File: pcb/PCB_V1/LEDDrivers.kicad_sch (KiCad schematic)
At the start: 57 parts, among them J711 LED1 / large 16S18P panel, J721 LED2 / strip 1, J731 LED3 / strip 2, Q711 100 V N-MOSFET / MPN pending, Q721 100 V N-MOSFET / MPN pending, Q731 100 V N-MOSFET / MPN pending, U710 LT3756, U720 LT3756, U730 LT3756

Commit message: pcb: repair LED current path and add boost energy storage
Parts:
- added C715, C725, C735: 22u / 25 V X7R / effective >=10u, Capacitor_SMD:C_1210_3225Metric, symbol Device:C
- added C716, C717, C726, C727, C736, C737: 10u / 100 V X7R / effective >=4.7u, Capacitor_SMD:C_1210_3225Metric, symbol Device:C
- C712, C722, C732: value 2.2u / 16 V -> 4.7u / 16 V X7R; footprint Capacitor_SMD:C_0603_1608Metric -> Capacitor_SMD:C_0805_2012Metric
- R711, R721, R731: value 20k / ~500 kHz preliminary -> 21k / 500 kHz nominal
- R712, R722, R732: value 10k -> 33k / CTRL upper
- R713, R723, R733: value 10k -> 100k / CTRL lower
- R715: value 0.1 / current limit sense -> 0.012 / 1% / >=2W
- R725, R735: value 0.1 / current limit sense -> 0.047 / 1% / >=1W; footprint Resistor_SMD:R_0603_1608Metric -> Resistor_SMD:R_2512_6332Metric
- U710, U720, U730: value LT3756 -> LT3756EMSE-2#PBF
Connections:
- net LED1_SENSE_P is gone; now on net LED1_OUT: R716.1, U710.4 (ISP)
- net LED2_SENSE_P is gone; now on net LED2_OUT: R726.1, U720.4 (ISP)
- net LED3_SENSE_P is gone; now on net LED3_OUT: R736.1, U730.4 (ISP)
- net +12V_LED: now also C715.1, C725.1, C735.1
- net GND: now also C715.2, C716.2, C717.2, C725.2, C726.2, C727.2, C735.2, C736.2, C737.2
- net LED1_OUT: now also C716.1, C717.1
- net LED2_OUT: now also C726.1, C727.1
- net LED3_OUT: now also C736.1, C737.1

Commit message: pcb: correct power MOSFET pin mapping and reverse input protection
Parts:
- Q711, Q721, Q731: symbol Transistor_FET:Q_NMOS_GDS -> GrowBox:NMOS_PowerPAK_Candidate
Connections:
- net LED1_GATE: now also Q711.4 (G); no longer Q711.1 (G)
- net LED1_IS: now also Q711.1 (S), Q711.2 (S)
- net LED1_SW: now also Q711.5 (D); no longer Q711.2 (D)
- net LED2_GATE: now also Q721.4 (G); no longer Q721.1 (G)
- net LED2_IS: now also Q721.1 (S), Q721.2 (S)
- net LED2_SW: now also Q721.5 (D); no longer Q721.2 (D)
- net LED3_GATE: now also Q731.4 (G); no longer Q731.1 (G)
- net LED3_IS: now also Q731.1 (S), Q731.2 (S)
- net LED3_SW: now also Q731.5 (D); no longer Q731.2 (D)
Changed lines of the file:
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@@
 		(title "07 - Three independent LED constant-current boost channels")
 		(date "2026-09-26")
-		(rev "0.6-DRAFT")
+		(rev "0.7-DRAFT")
 		(company "GrowBox controller")
 		(comment 1 "Logic first; power loads not yet implemented")
@@
 	)
 	(symbol
-		(lib_id "Transistor_FET:Q_NMOS_GDS")
+		(lib_id "GrowBox:NMOS_PowerPAK_Candidate")
 		(at 121.92 114.3 0)
 		(unit 1)
@@
 			)
 		)
+		(pin "4"
+		)
+		(pin "5"
+		)
 		(pin "1"
 		)
@@
 	)
 	(symbol
-		(lib_id "Transistor_FET:Q_NMOS_GDS")
+		(lib_id "GrowBox:NMOS_PowerPAK_Candidate")
 		(at 121.92 289.56 0)
 		(unit 1)
@@
 			)
 		)
+		(pin "4"
+		)
+		(pin "5"
+		)
 		(pin "1"
 		)
@@
 	)
 	(symbol
-		(lib_id "Transistor_FET:Q_NMOS_GDS")
+		(lib_id "GrowBox:NMOS_PowerPAK_Candidate")
 		(at 121.92 464.82 0)
 		(unit 1)
@@
 			)
 		)
+		(pin "4"
+		)
+		(pin "5"
+		)
 		(pin "1"

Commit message: pcb: match LED MOSFET packages and export complete schematic BOM
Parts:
- Q711, Q721, Q731: value 100 V N-MOSFET / MPN pending -> Si7454DDP-T1-GE3; footprint Package_SO:PowerPAK_SO-8L_Single -> Package_SO:PowerPAK_SO-8_Single
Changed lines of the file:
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@@
 			)
 		)
-		(property "Value" "100 V N-MOSFET / MPN pending"
+		(property "Value" "Si7454DDP-T1-GE3"
 			(at 121.92 104.14 0)
 			(show_name no)
@@
 			)
 		)
-		(property "Footprint" "Package_SO:PowerPAK_SO-8L_Single"
+		(property "Footprint" "Package_SO:PowerPAK_SO-8_Single"
 			(at 121.92 114.3 0)
 			(hide yes)
@@
 			)
 		)
-		(property "Datasheet" ""
+		(property "Datasheet" "https://www.vishay.com/docs/67883/si7454ddp.pdf"
 			(at 121.92 114.3 0)
 			(hide yes)
@@
 			)
 		)
-		(property "Value" "100 V N-MOSFET / MPN pending"
+		(property "Value" "Si7454DDP-T1-GE3"
 			(at 121.92 279.4 0)
 			(show_name no)
@@
 			)
 		)
-		(property "Footprint" "Package_SO:PowerPAK_SO-8L_Single"
+		(property "Footprint" "Package_SO:PowerPAK_SO-8_Single"
 			(at 121.92 289.56 0)
 			(hide yes)
@@
 			)
 		)
-		(property "Datasheet" ""
+		(property "Datasheet" "https://www.vishay.com/docs/67883/si7454ddp.pdf"
 			(at 121.92 289.56 0)
 			(hide yes)
@@
 			)
 		)
-		(property "Value" "100 V N-MOSFET / MPN pending"
+		(property "Value" "Si7454DDP-T1-GE3"
 			(at 121.92 454.66 0)
 			(show_name no)
@@
 			)
 		)
-		(property "Footprint" "Package_SO:PowerPAK_SO-8L_Single"
+		(property "Footprint" "Package_SO:PowerPAK_SO-8_Single"
 			(at 121.92 464.82 0)
 			(hide yes)
@@
 			)
 		)
-		(property "Datasheet" ""
+		(property "Datasheet" "https://www.vishay.com/docs/67883/si7454ddp.pdf"
 			(at 121.92 464.82 0)
 			(hide yes)

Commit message: pcb: replace LT3756 with lower-cost AL8853 LED channels
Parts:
- removed R710, R720, R730: 6.34k / FB divider, Resistor_SMD:R_0603_1608Metric, symbol Device:R
- removed R719, R729, R739: 249k / FB divider, Resistor_SMD:R_0603_1608Metric, symbol Device:R
- added C700: 100n 16V, Capacitor_SMD:C_0603_1608Metric, symbol Device:C
- added R701, R702, R703: 47k, Resistor_SMD:R_0603_1608Metric, symbol Device:R
- added U700: SN74LVC1G08DBVR, Package_TO_SOT_SMD:SOT-23-5, symbol 74xGxx:74LVC1G08
- C711, C721, C731: value 100n / 25 V -> 1u 25V X7R; footprint Capacitor_SMD:C_0603_1608Metric -> Capacitor_SMD:C_0805_2012Metric
- C712, C722, C732: value 4.7u / 16 V X7R -> 100p / comp tune; footprint Capacitor_SMD:C_0805_2012Metric -> Capacitor_SMD:C_0603_1608Metric
- C713, C723, C733: value 100n soft-start -> 100p / CS tune
- C714, C724, C734: value 2.2n compensation -> 220n / comp tune
- C715, C725, C735: value 22u / 25 V X7R / effective >=10u -> 22u 25V X7R
- C716, C717, C726, C727, C736, C737: value 10u / 100 V X7R / effective >=4.7u -> 10u 100V X7R
- D711, D721, D731: value 100 V Schottky / MPN pending -> 100V 5A / MPN TBD
- J711: value LED1 / large 16S18P panel -> LED +/- (return isolated); footprint TerminalBlock_WAGO:TerminalBlock_WAGO_2601-1102_1x02_P3.50mm_Horizontal -> TerminalBlock_Phoenix:TerminalBlock_Phoenix_MKDS-1,5-2-5.08_1x02_P5.08mm_Horizontal
- J721: value LED2 / strip 1 -> LED +/- (return isolated); footprint TerminalBlock_WAGO:TerminalBlock_WAGO_2601-1102_1x02_P3.50mm_Horizontal -> TerminalBlock_Phoenix:TerminalBlock_Phoenix_MKDS-1,5-2-5.08_1x02_P5.08mm_Horizontal
- J731: value LED3 / strip 2 -> LED +/- (return isolated); footprint TerminalBlock_WAGO:TerminalBlock_WAGO_2601-1102_1x02_P3.50mm_Horizontal -> TerminalBlock_Phoenix:TerminalBlock_Phoenix_MKDS-1,5-2-5.08_1x02_P5.08mm_Horizontal
- L711: value 22uH / Isat >= 10 A -> 47u / Isat>=14A / TBD; footprint Inductor_SMD:L_10.4x10.4_H4.8 -> Inductor_SMD:L_Bourns_SRP1245A
- L721, L731: value 47uH / Isat >= 3 A -> 100u / Isat>=5A / TBD; footprint Inductor_SMD:L_10.4x10.4_H4.8 -> Inductor_SMD:L_Bourns_SRP1245A
- Q711: value Si7454DDP-T1-GE3 -> SiR106ADP-T1-RE3
- R711, R721, R731: value 21k / 500 kHz nominal -> 10R
- R712, R722, R732: value 33k / CTRL upper -> 1k / slope tune
- R713, R723, R733: value 100k / CTRL lower -> 100k
- R714, R724, R734: value 10k -> 10k / comp tune
- R715: value 0.012 / 1% / >=2W -> 0.027 1% >=2W
- R716: value 0.091 / 1% -> 0.182 1% >=1W
- R717, R727, R737: value 249k / OVP divider -> 316k 1%
- R718, R728, R738: value 6.34k / OVP divider -> 10k 1%
- R725, R735: value 0.047 / 1% / >=1W -> 0.10 1% >=1W
- R726, R736: value 0.40 / 1% -> 0.80 1% >=0.25W; footprint Resistor_SMD:R_0603_1608Metric -> Resistor_SMD:R_1206_3216Metric
- U710, U720, U730: value LT3756EMSE-2#PBF -> AL8853S-13; footprint Package_SO:MSOP-16-1EP_3x4.039mm_P0.5mm_EP1.651x2.845mm_ThermalVias -> Package_SO:SOIC-8_3.9x4.9mm_P1.27mm; symbol Driver_LED:LT3756xMSE -> GrowBox:AL8853
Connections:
- net +12V_LED: now also U710.1 (VIN), U720.1 (VIN), U730.1 (VIN); no longer U710.14 (VIN), U720.14 (VIN), U730.14 (VIN)
- net GND: now also R716.2, R726.2, R736.2, U710.3 (GND), U720.3 (GND), U730.3 (GND), C700.2, R701.2, R702.2, R703.2, U700.3 (GND); no longer J711.2 (Pin_2), J721.2 (Pin_2), J731.2 (Pin_2), R711.2, R713.2, R721.2, R723.2, R731.2, R733.2, U710.17 (GND), U720.17 (GND), U730.17 (GND)
- net LED1_COMP: now also C712.1, U710.6 (COMP); no longer U710.5 (VC)
- net LED1_GATE: now also R711.2, R713.1; no longer U710.16 (GATE)
- net LED1_OUT: now also J711.1 (Pin_1); no longer R716.1, U710.4 (ISP)
- net LED1_OVP: now also U710.7 (OVP)
- net LED2_COMP: now also C722.1, U720.6 (COMP); no longer U720.5 (VC)
- net LED2_GATE: now also R721.2, R723.1; no longer U720.16 (GATE)
- net LED2_OUT: now also J721.1 (Pin_1); no longer R726.1, U720.4 (ISP)
- net LED2_OVP: now also U720.7 (OVP)
- net LED3_COMP: now also C732.1, U730.6 (COMP); no longer U730.5 (VC)
- net LED3_GATE: now also R731.2, R733.1; no longer U730.16 (GATE)
- net LED3_OUT: now also J731.1 (Pin_1); no longer R736.1, U730.4 (ISP)
- net LED3_OVP: now also U730.7 (OVP)
- net LIGHT_ENABLE: now also R702.1, U700.2; no longer U710.12 (~{SHDN}/UVLO), U720.12 (~{SHDN}/UVLO), U730.12 (~{SHDN}/UVLO)
- net LIGHT_PWM: now also R701.1, U700.1; no longer U710.8 (PWM), U720.8 (PWM), U730.8 (PWM)
- removed net LED1_CTRL: R712.2, R713.1, U710.6 (CTRL)
- net LED1_FB renamed LED1_DRV
- net LED1_DRV: now also R711.1
- removed net LED1_INTVCC: C712.1, U710.13 (INTVCC)
- net LED1_IS renamed LED1_SOURCE
- net LED1_SOURCE: now also R712.1, R713.2; no longer U710.15 (SENSE)
- removed net LED1_LEDPLUS: J711.1 (Pin_1), R716.2, U710.3 (ISN)
- removed net LED1_RT: R711.1, U710.11 (RT)
- net LED1_SS renamed LED1_CS
- net LED1_CS: now also R712.2, U710.4 (CS); no longer U710.10 (SS)
- removed net LED1_VREF: R712.1, U710.7 (VREF)
- removed net LED2_CTRL: R722.2, R723.1, U720.6 (CTRL)
- net LED2_FB renamed LED2_DRV
- net LED2_DRV: now also R721.1
- removed net LED2_INTVCC: C722.1, U720.13 (INTVCC)
- net LED2_IS renamed LED2_SOURCE
- net LED2_SOURCE: now also R722.1, R723.2; no longer U720.15 (SENSE)
- removed net LED2_LEDPLUS: J721.1 (Pin_1), R726.2, U720.3 (ISN)
- removed net LED2_RT: R721.1, U720.11 (RT)
- net LED2_SS renamed LED2_CS
- net LED2_CS: now also R722.2, U720.4 (CS); no longer U720.10 (SS)
- removed net LED2_VREF: R722.1, U720.7 (VREF)
- removed net LED3_CTRL: R732.2, R733.1, U730.6 (CTRL)
- net LED3_FB renamed LED3_DRV
- net LED3_DRV: now also R731.1
- removed net LED3_INTVCC: C732.1, U730.13 (INTVCC)
- net LED3_IS renamed LED3_SOURCE
- net LED3_SOURCE: now also R732.1, R733.2; no longer U730.15 (SENSE)
- removed net LED3_LEDPLUS: J731.1 (Pin_1), R736.2, U730.3 (ISN)
- removed net LED3_RT: R731.1, U730.11 (RT)
- net LED3_SS renamed LED3_CS
- net LED3_CS: now also R732.2, U730.4 (CS); no longer U730.10 (SS)
- removed net LED3_VREF: R732.1, U730.7 (VREF)
- new net +3V3: C700.1, U700.5 (VCC)
- new net LED1_RETURN: J711.2 (Pin_2), R716.1, U710.5 (FB)
- new net LED2_RETURN: J721.2 (Pin_2), R726.1, U720.5 (FB)
- new net LED3_RETURN: J731.2 (Pin_2), R736.1, U730.5 (FB)
- new net LED_DIM: R703.1, U700.4, U710.8 (PWM), U720.8 (PWM), U730.8 (PWM)
- no-connect marks 6 -> 0
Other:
- note added: "0.9 COST-DOWN DRAFT: component budget <= USD 30 target, not a purchase quote. AL8853 replaces LT3756."
- note added: "CH1: 1.099 A nominal / panel"
- note added: "CH2: 0.250 A nominal / strip"
- note added: "CH3: 0.250 A nominal / strip"
- note added: "DRAFT: 120 kHz; OVP nominal 65.2 V. All output power parts >=100 V. Inductor/diode footprints are placeholders."
- note added: "Do not connect LED- to GND or join LED returns. Output short protection needs branch fuses/disconnect; boost diode conducts at shutdown."
- note added: "L saturation/current rating, slope compensation, transient response, output capacitance and thermal performance require verification."
- note added: "PWM 20 kHz initial / analog current dimming. Enable low or reset: DIM low. LED returns MUST remain separate."
- note added: "THREE INDEPENDENT CONSTANT-CURRENT BOOST CHANNELS / COMMON DIMMING"
- note removed: "0.4 DRAFT. Target currents: CH1 1.10 A, CH2 0.25 A, CH3 0.25 A; total nominal 76.8 W at 48 V."
- note removed: "All three channels share LIGHT_PWM and LIGHT_ENABLE from ESP32 but have independent inductors, MOSFETs, current-sense resistors, OVP and LED connectors. Keep switch loops compact and separate from SENSE/FB routing."
- note removed: "CHANNEL 1: large 16S18P panel / 1.10 A target / 52.8 W target"
- note removed: "CHANNEL 2: strip 1 / 0.25 A target / 12.0 W target"
- note removed: "CHANNEL 3: strip 2 / 0.25 A target / 12.0 W target"
- note removed: "LED / 12 V -> 40..48 V / THREE INDEPENDENT CONSTANT-CURRENT BOOST CHANNELS"
- note removed: "RCS 0.091 / 1%; high-side shunt before LED+. Tune after measuring actual LED Vf and current. R715 is switch-current sense, not LED current sense. OVP/FB dividers are preliminary for 48 V operation; validate open-LED overshoot and compensation with the real panel."
- note removed: "RCS 0.40 / 1%; high-side shunt before LED+. Tune after measuring actual LED Vf and current. R725 is switch-current sense, not LED current sense. OVP/FB dividers are preliminary for 48 V operation; validate open-LED overshoot and compensation with the real panel."
- note removed: "RCS 0.40 / 1%; high-side shunt before LED+. Tune after measuring actual LED Vf and current. R735 is switch-current sense, not LED current sense. OVP/FB dividers are preliminary for 48 V operation; validate open-LED overshoot and compensation with the real panel."
- title: 07 - Three independent LED constant-current boost channels -> 07 - AL8853 cost-down LED drivers
- moved on the sheet: C711, C712, C713, C714, C715, C716, C717, C721, C722, C723, C724, C725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

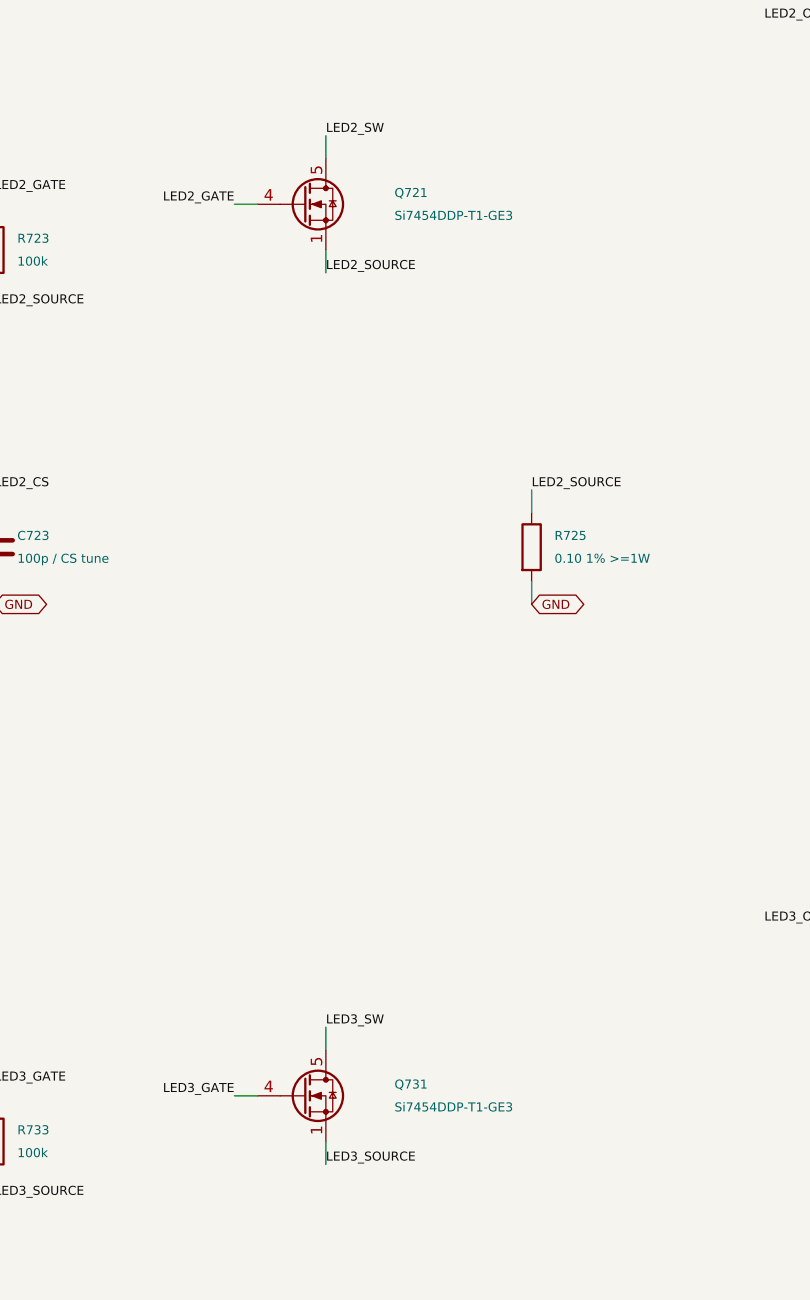
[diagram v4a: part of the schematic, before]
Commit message: pcb: replace strip LED MOSFETs with DMT10H009LK3 DPAK parts
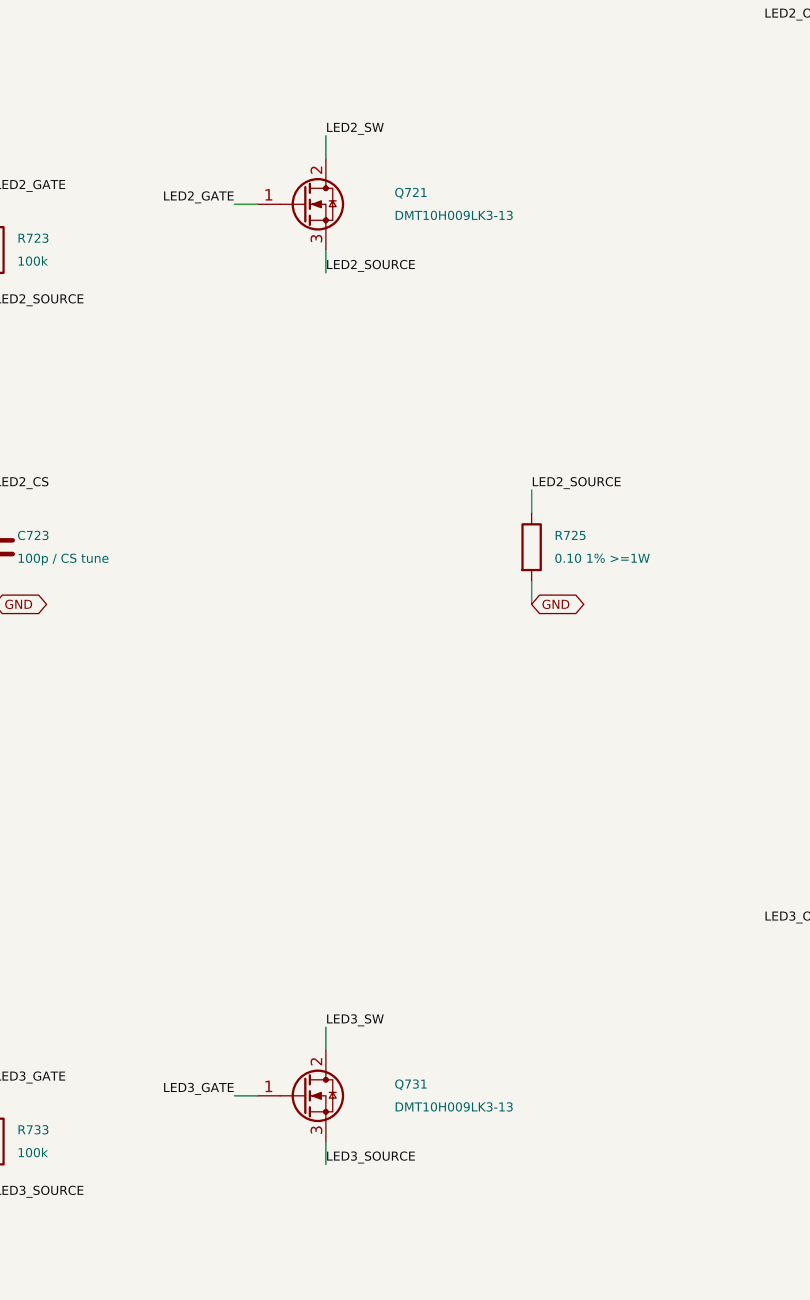
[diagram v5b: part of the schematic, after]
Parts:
- Q721, Q731: value Si7454DDP-T1-GE3 -> DMT10H009LK3-13; footprint Package_SO:PowerPAK_SO-8_Single -> GrowBox:Diodes_TO252_DMT10H009LK3; symbol GrowBox:NMOS_PowerPAK_Candidate -> GrowBox:DMT10H009LK3
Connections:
- net LED2_GATE: now also Q721.1 (G); no longer Q721.4 (G)
- net LED2_SOURCE: no longer Q721.1 (S), Q721.2 (S)
- net LED2_SW: now also Q721.2 (D); no longer Q721.5 (D)
- net LED3_GATE: now also Q731.1 (G); no longer Q731.4 (G)
- net LED3_SOURCE: no longer Q731.1 (S), Q731.2 (S)
- net LED3_SW: now also Q731.2 (D); no longer Q731.5 (D)
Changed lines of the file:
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@@
 		(title "07 - AL8853 cost-down LED drivers")
 		(date "2026-09-27")
-		(rev "0.9-DRAFT")
+		(rev "0.10-DRAFT")
 		(company "GrowBox controller")
 		(comment 1 "AL8853 cost-down prototype; not fabrication ready")
@@
 	)
 	(symbol
-		(lib_id "GrowBox:NMOS_PowerPAK_Candidate")
+		(lib_id "GrowBox:DMT10H009LK3")
 		(at 224.79 218.44 0)
 		(unit 1)
@@
 			)
 		)
-		(property "Value" "Si7454DDP-T1-GE3"
+		(property "Value" "DMT10H009LK3-13"
 			(at 234.95 219.71 0)
 			(show_name no)
@@
 			)
 		)
-		(property "Footprint" "Package_SO:PowerPAK_SO-8_Single"
+		(property "Footprint" "GrowBox:Diodes_TO252_DMT10H009LK3"
 			(at 224.79 218.44 0)
 			(hide yes)
@@
 			)
 		)
-		(property "Datasheet" ""
+		(property "Datasheet" "https://www.diodes.com/datasheet/download/DMT10H009LK3.pdf"
 			(at 224.79 218.44 0)
 			(hide yes)
@@
 			)
 		)
-		(pin "4"
-		)
-		(pin "5"
-		)
 		(pin "1"
 		)
@@
 	)
 	(symbol
-		(lib_id "GrowBox:NMOS_PowerPAK_Candidate")
+		(lib_id "GrowBox:DMT10H009LK3")
 		(at 224.79 317.5 0)
 		(unit 1)
@@
 			)
 		)
-		(property "Value" "Si7454DDP-T1-GE3"
+		(property "Value" "DMT10H009LK3-13"
 			(at 234.95 318.77 0)
 			(show_name no)
@@
 			)
 		)
-		(property "Footprint" "Package_SO:PowerPAK_SO-8_Single"
+		(property "Footprint" "GrowBox:Diodes_TO252_DMT10H009LK3"
 			(at 224.79 317.5 0)
 			(hide yes)
@@
 			)
 		)
-		(property "Datasheet" ""
+		(property "Datasheet" "https://www.diodes.com/datasheet/download/DMT10H009LK3.pdf"
 			(at 224.79 317.5 0)
 			(hide yes)
@@
 			)
 		)
-		(pin "4"
-		)
-		(pin "5"
-		)
 		(pin "1"
